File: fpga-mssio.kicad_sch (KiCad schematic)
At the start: 14 parts, among them U1 MPFS250T-FCVG484

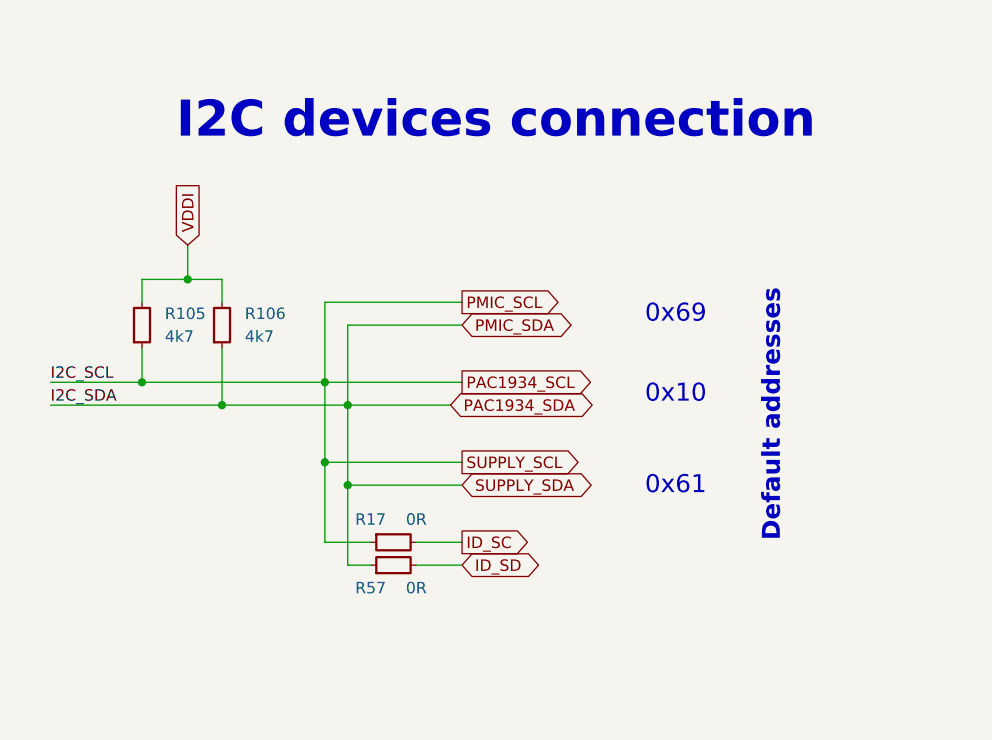
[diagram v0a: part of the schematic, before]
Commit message: [#57505] Continue migration to hierarchical schematic
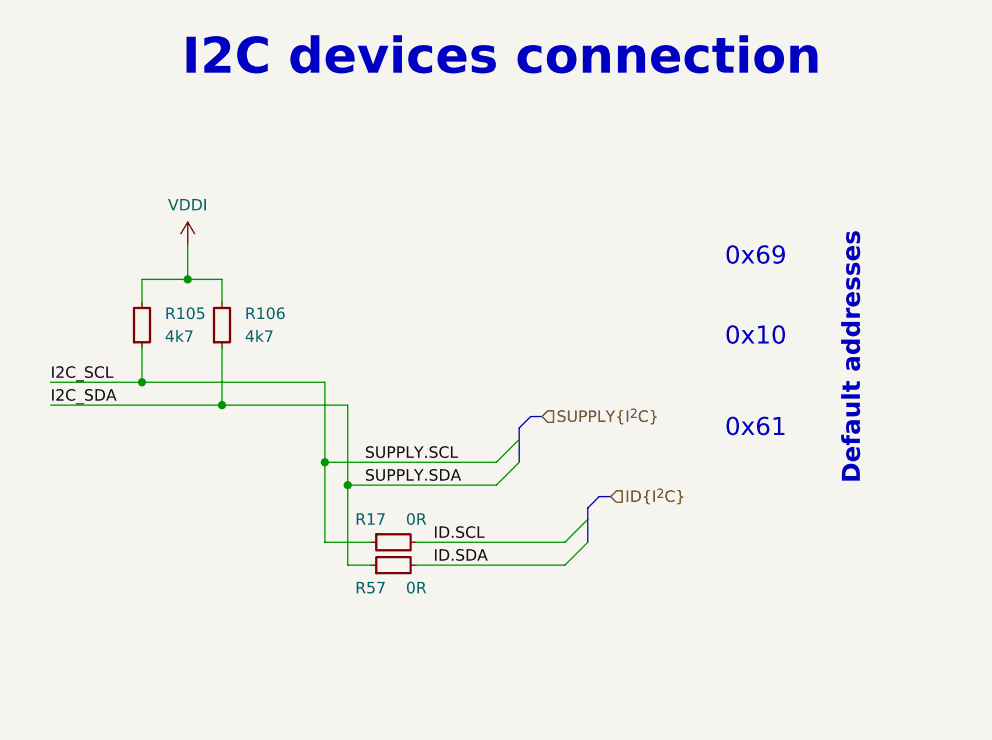
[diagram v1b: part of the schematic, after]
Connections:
- net ID_SC renamed ID.SCL
- net ID_SD renamed ID.SDA
- net PAC1934_SCL renamed I2C_SCL
- net PAC1934_SDA renamed I2C_SDA

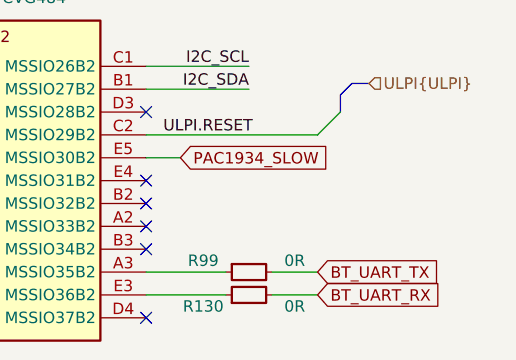
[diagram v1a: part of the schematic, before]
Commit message: [#57422] Add ETH PHY strap, WL_BT UART level shifter, fiducials, remove BYP_EN
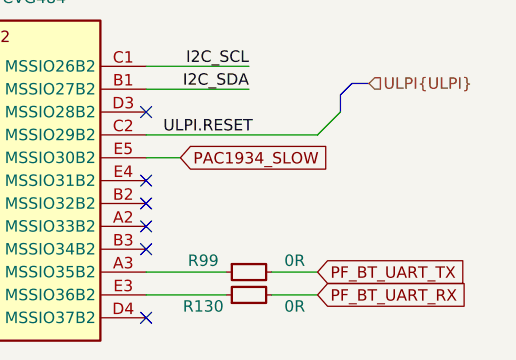
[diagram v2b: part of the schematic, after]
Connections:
- net BT_UART_RX renamed PF_BT_UART_RX
- net BT_UART_TX renamed PF_BT_UART_TX
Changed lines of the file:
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@@
     (effects (font (size 1.27 1.27)) (justify right bottom))
   )
-  (global_label "BT_UART_TX" (shape input) (at 351.155 210.185 0) (fields_autoplaced)
+  (global_label "PF_BT_UART_TX" (shape input) (at 351.155 210.185 0) (fields_autoplaced)
     (effects (font (size 1.27 1.27)) (justify left))
-    (property "Intersheetrefs" "${INTERSHEET_REFS}" (at 365.1468 210.185 0)
+    (property "Intersheetrefs" "${INTERSHEET_REFS}" (at 368.473 210.185 0)
       (effects (font (size 1.27 1.27)) (justify left))
     )
@@
     )
   )
-  (global_label "BT_UART_RX" (shape input) (at 351.155 212.725 0) (fields_autoplaced)
+  (global_label "PF_BT_UART_RX" (shape input) (at 351.155 212.725 0) (fields_autoplaced)
     (effects (font (size 1.27 1.27)) (justify left))
-    (property "Intersheetrefs" "${INTERSHEET_REFS}" (at 365.4492 212.725 0)
+    (property "Intersheetrefs" "${INTERSHEET_REFS}" (at 368.7754 212.725 0)
       (effects (font (size 1.27 1.27)) (justify left))
     )

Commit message: [#57505] Finish defining buses
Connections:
- net PF_BT_UART_RX renamed PF_BT.RX
- net PF_BT_UART_TX renamed PF_BT.TX
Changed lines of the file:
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@@
   (no_connect (at 332.105 200.025))
   (no_connect (at 332.105 202.565))
+  (bus_entry (at 368.935 210.185) (size 2.54 -2.54)
+    (stroke (width 0) (type default))
+  )
   (bus_entry (at 189.23 158.75) (size 2.54 -2.54)
     (stroke (width 0) (type default))
@@
     (stroke (width 0) (type default))
   )
+  (bus_entry (at 368.935 212.725) (size 2.54 -2.54)
+    (stroke (width 0) (type default))
+  )
   (bus_entry (at 189.23 147.32) (size 2.54 -2.54)
     (stroke (width 0) (type default))
@@
     (stroke (width 0) (type default))
   )
+  (bus (pts (xy 372.745 205.105) (xy 371.475 206.375))
+    (stroke (width 0) (type default))
+  )
   (wire (pts (xy 304.165 97.155) (xy 301.625 97.155))
     (stroke (width 0) (type default))
@@
     (stroke (width 0) (type default))
   )
+  (bus (pts (xy 371.475 207.645) (xy 371.475 210.185))
+    (stroke (width 0) (type default))
+  )
   (polyline (pts (xy 179.07 78.74) (xy 179.07 91.44))
     (stroke (width 0) (type default))
@@
     (stroke (width 0) (type default))
   )
+  (bus (pts (xy 371.475 206.375) (xy 371.475 207.645))
+    (stroke (width 0) (type default))
+  )
   (wire (pts (xy 158.75 66.04) (xy 198.755 66.04))
     (stroke (width 0) (type default))
@@
     (stroke (width 0) (type default))
   )
-  (wire (pts (xy 346.075 212.725) (xy 351.155 212.725))
+  (wire (pts (xy 346.075 212.725) (xy 368.935 212.725))
     (stroke (width 0) (type default))
   )
@@
     (stroke (width 0) (type default))
   )
-  (wire (pts (xy 346.075 210.185) (xy 351.155 210.185))
+  (wire (pts (xy 346.075 210.185) (xy 368.935 210.185))
     (stroke (width 0) (type default))
   )
@@
   )
   (bus (pts (xy 88.9 142.24) (xy 88.9 144.78))
+    (stroke (width 0) (type default))
+  )
+  (bus (pts (xy 372.745 205.105) (xy 374.015 205.105))
     (stroke (width 0) (type default))
   )
@@
     (effects (font (size 1.27 1.27)) (justify right bottom))
   )
+  (label "PF_BT.RX" (at 368.935 212.725 180) (fields_autoplaced)
+    (effects (font (size 1.27 1.27)) (justify right bottom))
+  )
   (label "SD.DAT3" (at 189.23 139.7 180) (fields_autoplaced)
     (effects (font (size 1.27 1.27)) (justify right bottom))
@@
     (effects (font (size 1.27 1.27)) (justify left bottom))
   )
+  (label "PF_BT.TX" (at 368.935 210.185 180) (fields_autoplaced)
+    (effects (font (size 1.27 1.27)) (justify right bottom))
+  )
   (label "MEM.DAT1" (at 89.535 71.12 0) (fields_autoplaced)
     (effects (font (size 1.27 1.27)) (justify left bottom))
@@
   (label "SD.DAT0" (at 189.23 142.24 180) (fields_autoplaced)
     (effects (font (size 1.27 1.27)) (justify right bottom))
-  )
-  (global_label "PF_BT_UART_TX" (shape input) (at 351.155 210.185 0) (fields_autoplaced)
-    (effects (font (size 1.27 1.27)) (justify left))
-    (property "Intersheetrefs" "${INTERSHEET_REFS}" (at 368.473 210.185 0)
-      (effects (font (size 1.27 1.27)) (justify left))
-    )
   )
   (global_label "PAC1934_SLOW" (shape input) (at 335.915 197.485 0) (fields_autoplaced)
@@
     )
   )
-  (global_label "PF_BT_UART_RX" (shape input) (at 351.155 212.725 0) (fields_autoplaced)
-    (effects (font (size 1.27 1.27)) (justify left))
-    (property "Intersheetrefs" "${INTERSHEET_REFS}" (at 368.7754 212.725 0)
-      (effects (font (size 1.27 1.27)) (justify left))
-    )
-  )
   (hierarchical_label "ID{I^{2}C}" (shape input) (at 330.835 89.535 0) (fields_autoplaced)
     (effects (font (size 1.27 1.27)) (justify left))
   )
+  (hierarchical_label "PF_BT{UART}" (shape input) (at 374.015 205.105 0) (fields_autoplaced)
+    (effects (font (size 1.27 1.27)) (justify left))
+  )

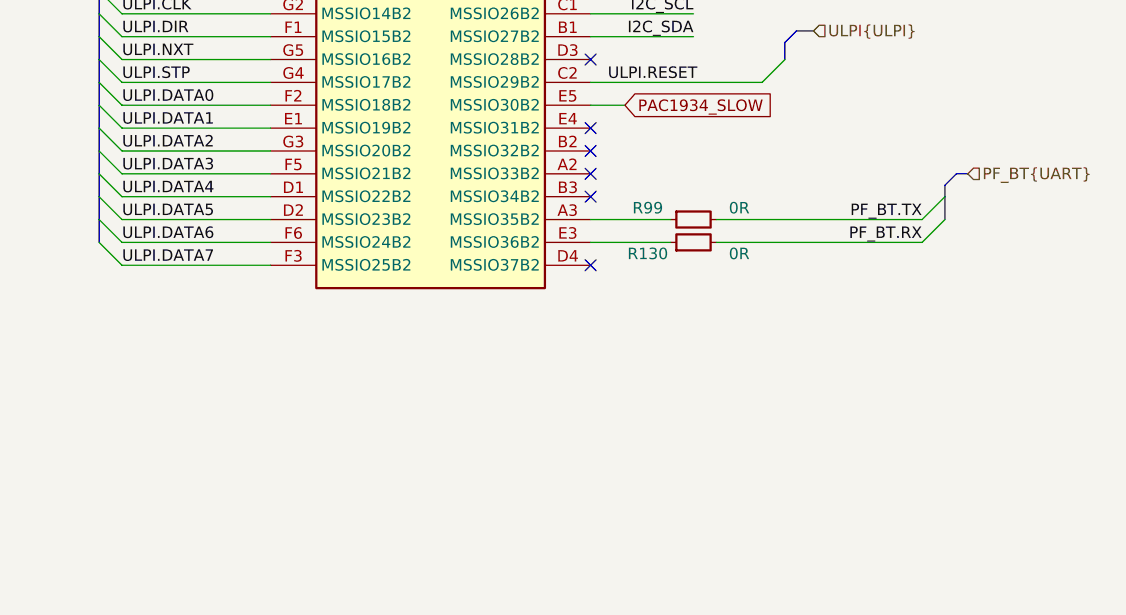
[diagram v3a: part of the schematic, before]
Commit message: [#57505] Finish migration to hierarchical structure
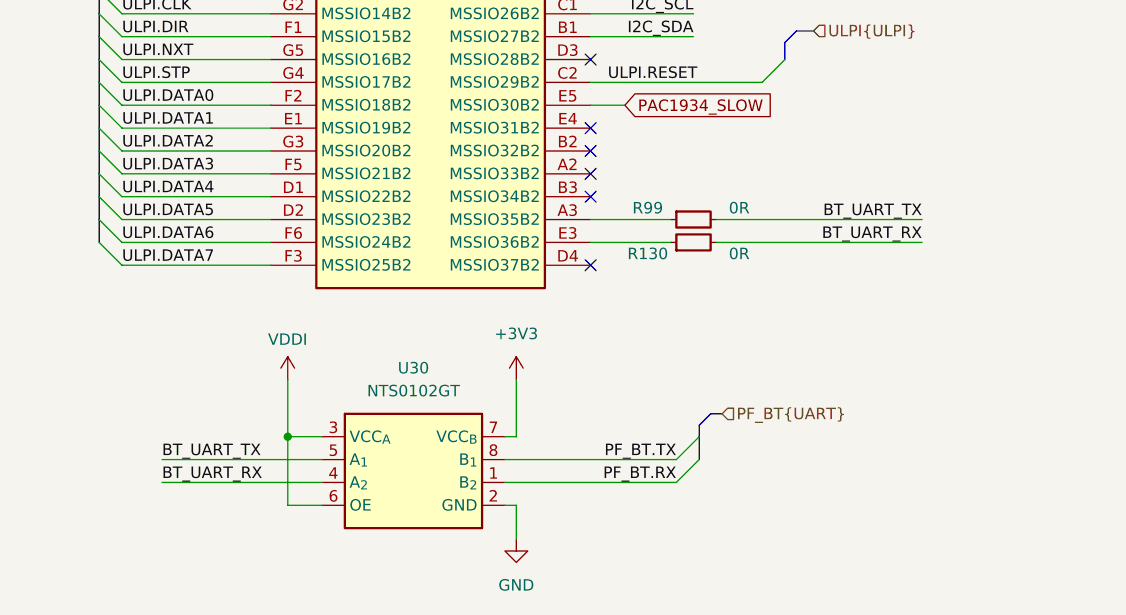
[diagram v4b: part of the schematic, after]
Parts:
- added U30: NTS0102_XSON, antmicro-footprints:XSON-8_1x1.95mm_P0.5mm, symbol antmicroLogicTranslatorsLevelShifters:NTS0102_XSON
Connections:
- net PF_BT.RX: now also U30.1 (B_{2}); no longer R130.2
- net PF_BT.TX: now also U30.8 (B_{1}); no longer R99.2
- net VDDI: now also U30.3 (VCC_{A}), U30.6 (OE)
- new net +3V3: U30.7 (VCC_{B})
- new net BT_UART_RX: R130.2, U30.4 (A_{2})
- new net BT_UART_TX: R99.2, U30.5 (A_{1})
- new net GND: U30.2 (GND)

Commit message: [#57422] Finishing touches
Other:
- note removed: "0x10"
- note removed: "0x61"
- note removed: "0x69"
- note removed: "Default addresses"
- note removed: "I2C devices connection"
- moved on the sheet: R105, R106, R130, R17, R22, R23, R24, R25, R26, R27, R53, R57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

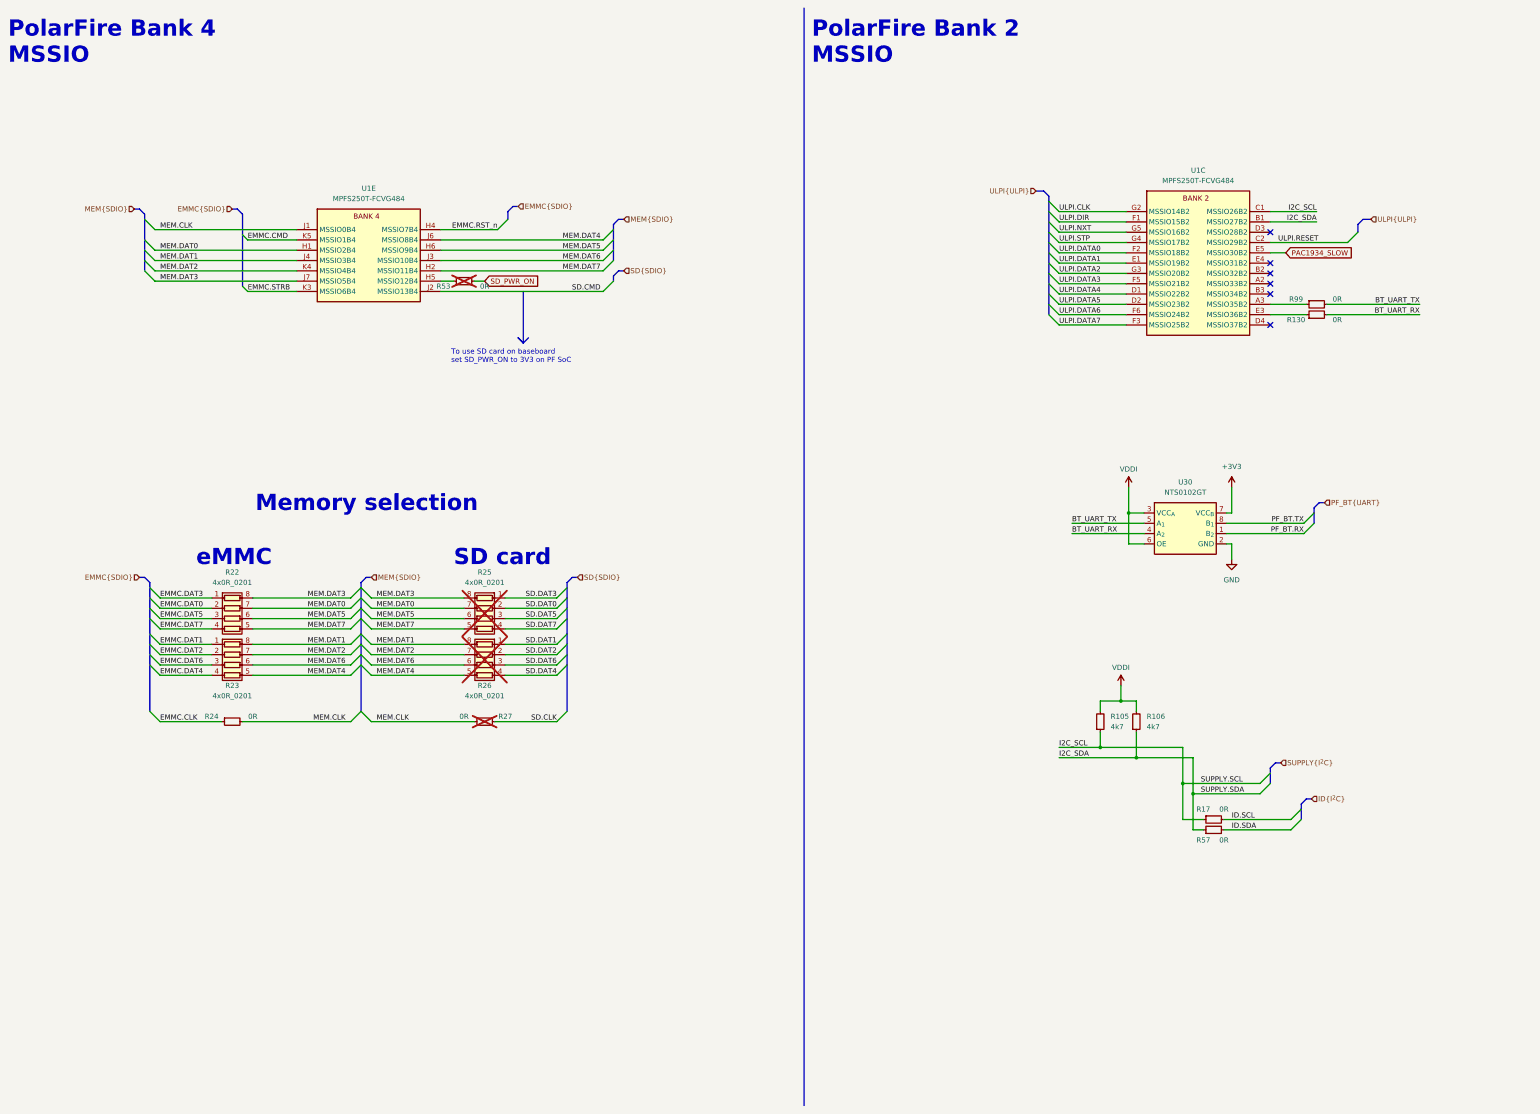
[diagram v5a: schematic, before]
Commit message: [#57422] Align schematics
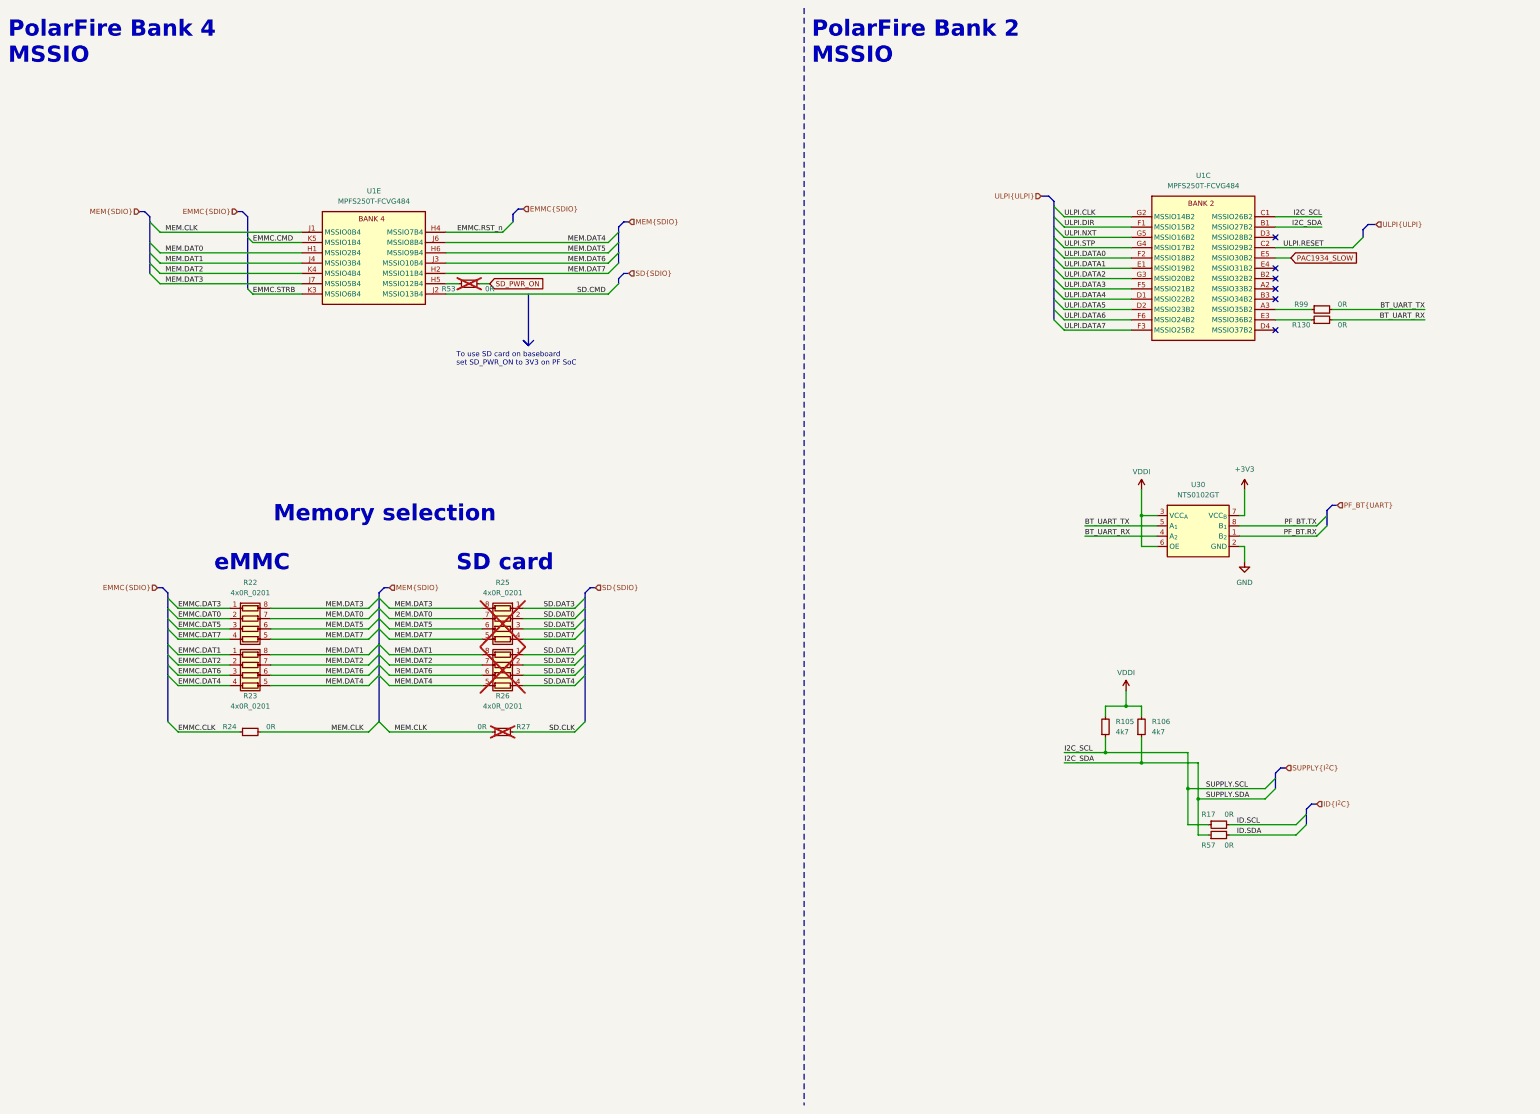
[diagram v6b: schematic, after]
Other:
- moved on the sheet: R105, R106, R130, R17, R22, R23, R24, R25, R26, R27, R53, R57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
